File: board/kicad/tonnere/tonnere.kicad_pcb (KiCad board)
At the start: 6 copper layers, 256.2 x 141.3 mm, 406 parts, among them J11 Conn_01x05, J13 STM USART TTL, J14 SPI CFG, J16 SPI SEL, J17 FPGA GPIO, J18 ESP PGM, J19 USB_A, J2 DE15_Pins_HighDensity_Mountin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, J20 73725-1180RLF, J21 FPGA JTAG, J22 ESP JTAG, J23 CONSOL, J24 73725-1180RLF, J25 73725-1180RLF, J26 I2C, J3 HDMI_A, J4 JA23331-HA6Q-4F, J5 PBI, J6 Conn_01x01, J7 PBI Option, J8 STM GPIO, J9 STM SWD, Q1 BCX51, Q2 DMN2058U, Q3 2N7002, SW1 SA-0-102-C04-0004-WP, SW2 USB HS/FS, U1 PLT237/T10WH, U10 TPD8E003DQDR, U11 TPD8E003DQDR, U12 74LVC1G17, U13 TPD4E02B04DQA, U14 TPD8E003DQDR, U15 TPD8E003DQDR, U16 TPS62903RPJR, U17 TPS62903RPJR, U18 FSUSB42UMX-TP, U19 TPD8E003DQDR, U2 TPD4E02B04DQA, U20 PCM5102A, U21 USB3300-EZK, U22 FSUSB42UMX-TP, U23 TPS62903RPJR, U24 THS7316DR, U25 STM32F407ZGTx, U26 TPD8E003DQDR, U27 PCA9546APWR, U28 M25PX32-VMW, U29 TPD8E003DQDR, U3 TPD4E02B04DQA, U30 M25PX32-VMW, U31 SN74CB3T16211DGVR, U32 IS61WV204816BLL-10BLI, U33 SN74CB3T16211DGVR, U34 10CL040f484, U35 AP2553AW6-7, U36 SN74CB3T16211DGVR, U37 IS61WV204816BLL-10BLI, U38 SN74CB3T16211DGVR, U39 AP2553AW6-7, U4 TPD4E02B04DQA, U40 AP2553AW6-7, U41 ESP32-WROVER-E-N8R8, U42 AP2553AW6-7, U43 AS4C16M16SA, U44 TPD4E02B04DQA, U45 USB2514B_Bi, U46 TPD4E02B04DQA, U47 TPD4E02B04DQA, U48 TPD4E02B04DQA, U5 TPD4E02B04DQA, U6 TPD8E003DQDR, U7 TPD8E003DQDR, U8 TPD8E003DQDR, U9 TPD8E003DQDR, Y1 24MHz, Y2 8MHz, Y3 32.768KHz, Y4 25MHz, Y5 Si5351A-B-GT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

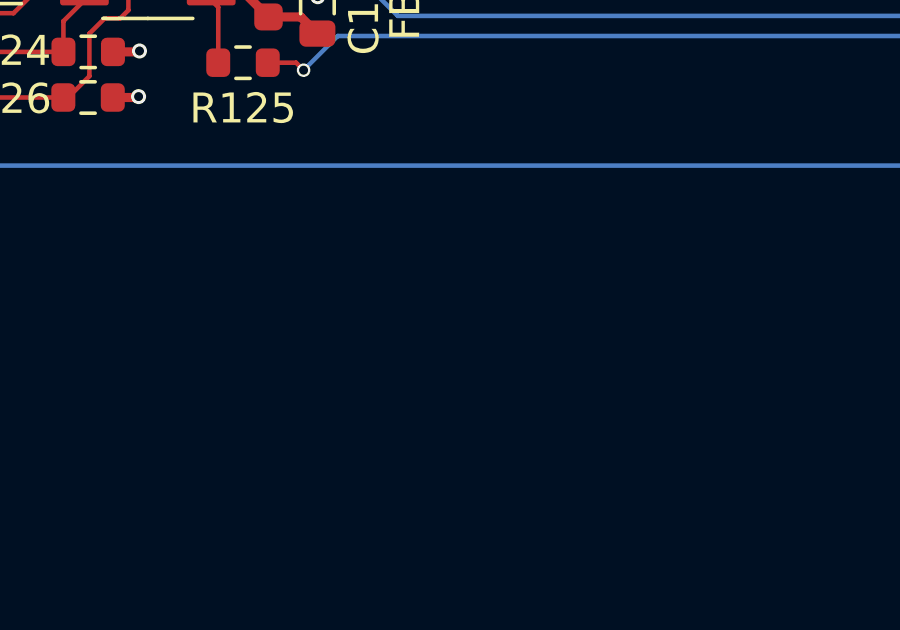
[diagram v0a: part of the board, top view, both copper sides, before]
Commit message: After simulation change video dac capacitance from 4.7pF to 1.8pF. Added square for JLCPCB qr code.
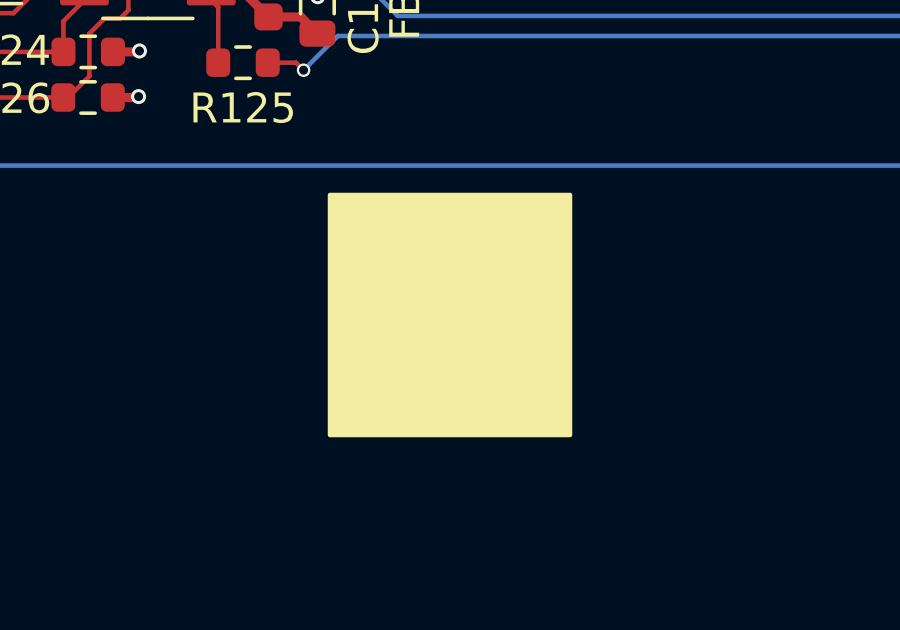
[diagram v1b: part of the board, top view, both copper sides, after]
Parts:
- C59, C61, C62: value 5pF -> 1.8pF
